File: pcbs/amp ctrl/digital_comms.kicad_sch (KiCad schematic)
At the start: 54 parts, among them J15 RJ45_Shielded, J17 RJ45_Shielded, J88 RJ45_Shielded, Q33 MMBT3904, Q34 MMBT3904, Q35 MMBT3906, Q38 MMBT3904, U21 74LVC2G17, U47 74LVC2G17, U62 FIN1028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

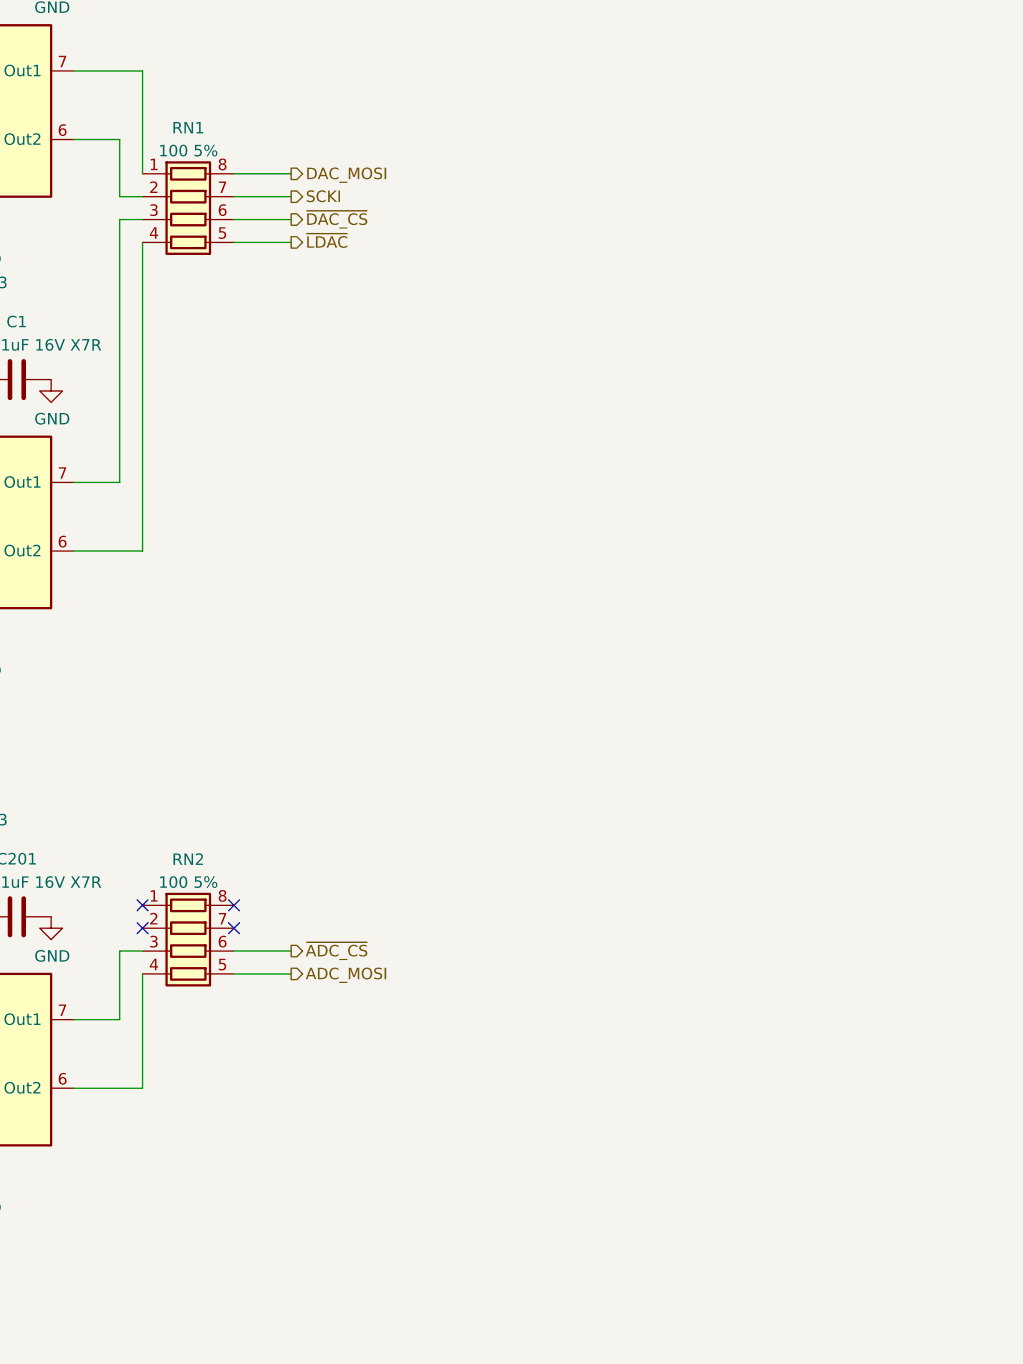
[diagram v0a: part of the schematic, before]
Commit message: BOM & reset fixes
Amp ctrl: changed name of "Manufacturer" field to "MPN" to work with Aisler
Amp ctrl: added part number to logic inverter, corrected various typos and part number problems
Backplane: added pull-down to Shutdown_Reset signal (#35)
Backplane: rethought Shutdown_Force circuit to make fail-safe (broken connections->shutdown), make work correctly (fixes #35)
Backplane: updated/corrected various schematic annotations
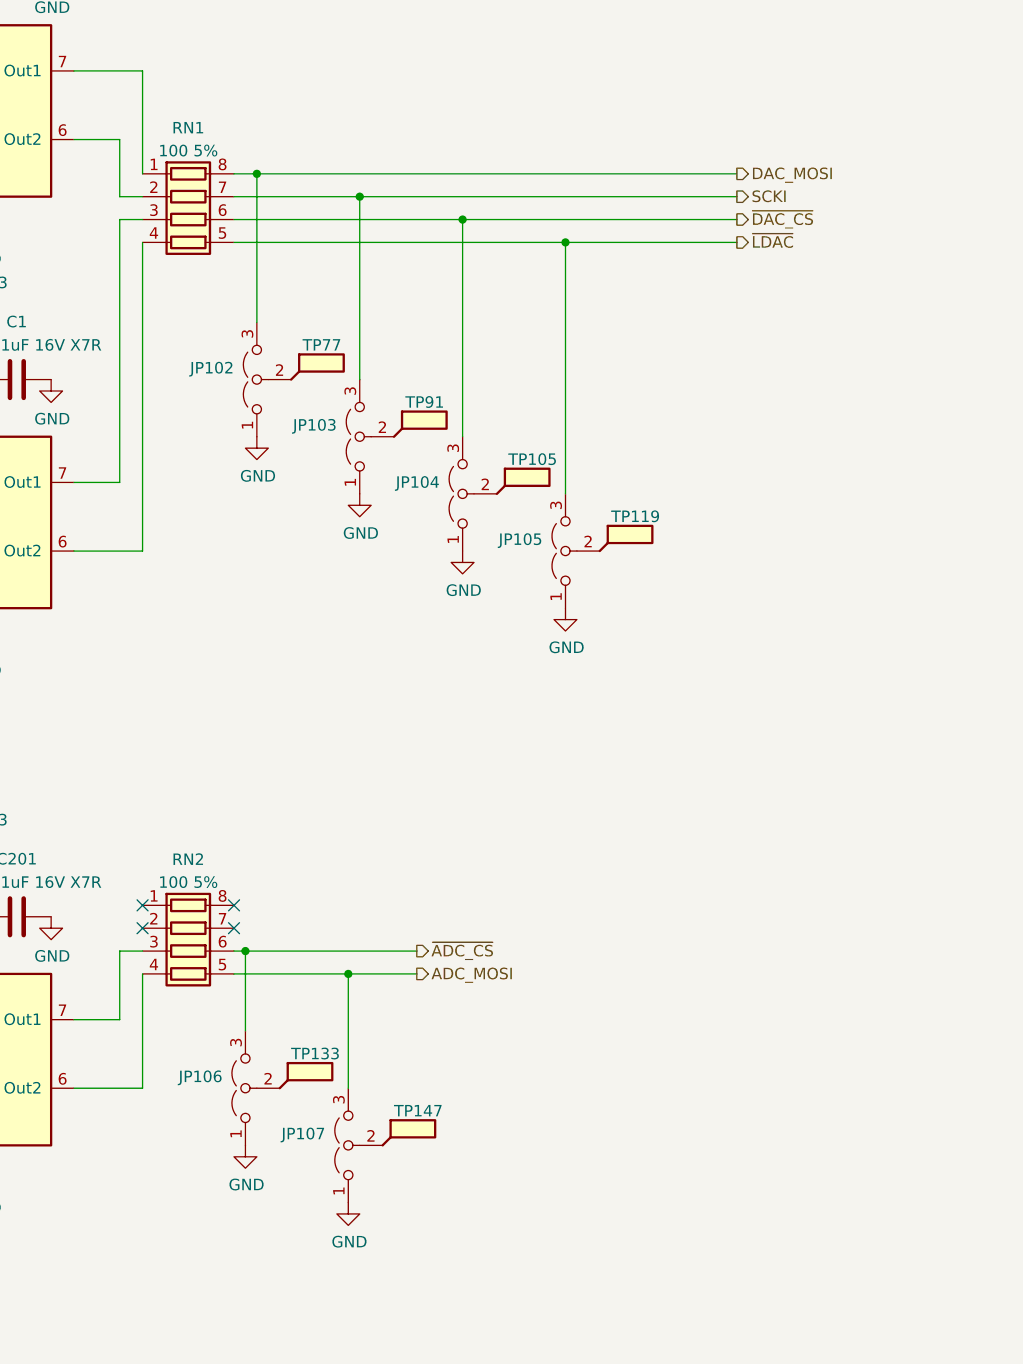
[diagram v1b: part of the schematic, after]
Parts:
- added JP102, JP103, JP104, JP105, JP106, JP107: Jumper_3_Open, Jumper:SolderJumper-3_P2.0mm_Open_TrianglePad1.0x1.5mm, symbol Jumper:Jumper_3_Open
- added TP105, TP119, TP133, TP147, TP77, TP91: TestPoint_Flag, TestPoint:TestPoint_Keystone_5019_Miniature, symbol Connector:TestPoint_Flag
- C1, C199, C200, C201, C253, C254, C255, C256: MPN (none) -> C0603C105K4RACTU; Part Number C0603C105K4RACTU -> (none)
- C198, C244, C56: MPN (none) -> C0603C102J5GACTU; Part Number C0603C102J5GACTU -> (none)
- C204: MPN (none) -> C0603C104K5RACTU; Part Number C0603C104K5RACTU -> (none)
- D29, D30, D65: MPN (none) -> BAS16J,115 / BAS16J,135; MPN Alt. (none) -> 1N4448WSF-7 / 1N4448WSFQ-7, 1N4448WS; Part Number BAS16J,115 / BAS16J,135 -> (none); Part Number Alt. 1N4448WSF-7 / 1N4448WSFQ-7, 1N4448WS -> (none)
- J15, J17, J88: MPN (none) -> 1-406541-8; MPN Alt. (none) -> 1-406541-5, 2-406541-1; Part Number 1-406541-8 -> (none); Part Number Alt. 1-406541-5, 2-406541-1 -> (none)
- JP71: now left out of the parts list
- Q33, Q34, Q38: MPN (none) -> MMBT3904-7-F; MPN Alt. (none) -> MMBT3904,215; Part Number MMBT3904-7-F -> (none); Part Number Alt. MMBT3904,215 -> (none)
- Q35: MPN (none) -> MMBT3906-7-F; MPN Alt. (none) -> MMBT3906,215; Part Number MMBT3906-7-F -> (none); Part Number Alt. MMBT3906,215 -> (none)
- R165, R285, R289: MPN (none) -> RK73H2ATTD4703F; Part Number RK73H2ATTD4703F -> (none)
- R166, R173, R174, R286: MPN (none) -> RK73H2ATTD1002F; Part Number RK73H2ATTE1002F -> (none)
- R175, R176, R178, R179, R180, R181: MPN (none) -> RK73H2ATTD4641F; Part Number RK73H2ATTD4641F -> (none)
- R177, R287: MPN (none) -> RK73H2ATTD1001F; Part Number RK73H2ATTDD1001F -> (none)
- R290, R293: MPN (none) -> RK73H2ATTD1003F; Part Number RK73H2ATTE1003F -> (none)
- RN1, RN2, RN3, RN4: MPN (none) -> 742C083101JP; MPN Alt. (none) -> CAT16-101J4LF; Part Number 742C083101JP -> (none); Part Number Alt. CAT16-101J4LF -> (none)
- RN21, RN22: MPN (none) -> 742C083333JP; MPN Alt. (none) -> CAT16-333J4LF; Part Number 742C083333JP -> (none); Part Number Alt. CAT16-333J4LF -> (none)
- U21, U47: MPN (none) -> 74LVC2G17GV,125; MPN Alt. (none) -> SN74LVC2G17DBVR / SN74LVC2G17DBVT, 74LVC2G17W6-7; Part Number 74LVC2G17GV,125 -> (none); Part Number Alt. SN74LVC2G17DBVR / SN74LVC2G17DBVT, 74LVC2G17W6-7 -> (none)
- U62, U63, U71: MPN (none) -> FIN1028MX; Part Number FIN1028MX -> (none)
- U64: MPN (none) -> FIN1047MTCX; Part Number FIN1047MTCX -> (none)
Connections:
- net ADC_MOSI: now also JP107.3 (B)
- net DAC_MOSI: now also JP102.3 (B)
- net GND: now also JP102.1 (A), JP103.1 (A), JP104.1 (A), JP105.1 (A), JP106.1 (A), JP107.1 (A)
- net SCKI: now also JP103.3 (B)
- net ~{ADC_CS}: now also JP106.3 (B)
- net ~{DAC_CS}: now also JP104.3 (B)
- net ~{LDAC}: now also JP105.3 (B)
- new net: JP104.2 (C), TP105.1
- new net: JP106.2 (C), TP133.1
- new net: JP102.2 (C), TP77.1
- new net: JP105.2 (C), TP119.1
- new net: JP107.2 (C), TP147.1
- new net: JP103.2 (C), TP91.1
